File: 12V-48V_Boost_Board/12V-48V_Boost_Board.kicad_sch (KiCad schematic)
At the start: 12 parts, among them J1 12V Input, J2 Input Current Sensing, J3 Output Current Sensing, J4 48V Output, J5 Output Measuring

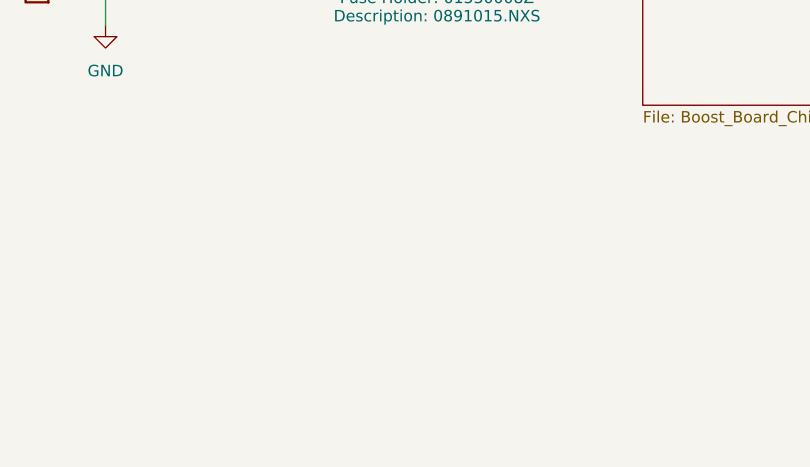
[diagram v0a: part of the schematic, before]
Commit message: Added mounting holes
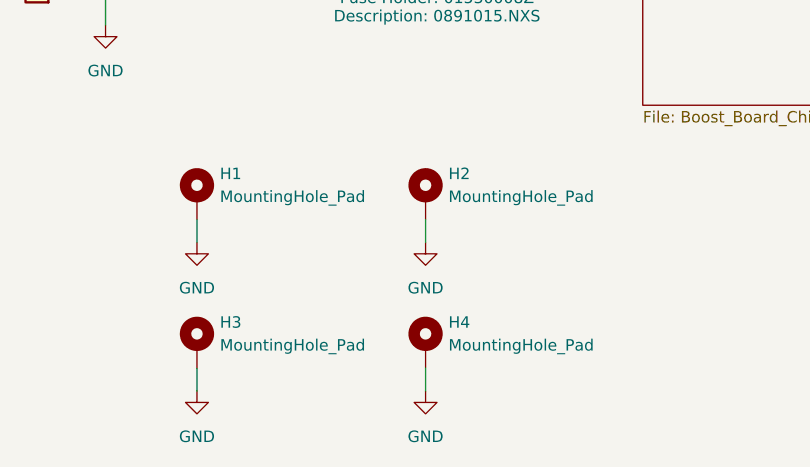
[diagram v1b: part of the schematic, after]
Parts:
- added H1, H2, H3, H4: MountingHole_Pad, MountingHole:MountingHole_3.2mm_M3_Pad, symbol Mechanical:MountingHole_Pad
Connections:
- net GND: now also H1.1, H2.1, H3.1, H4.1

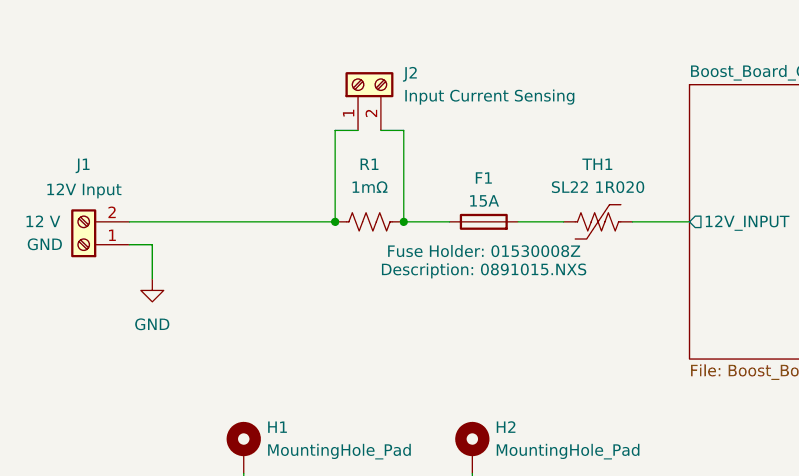
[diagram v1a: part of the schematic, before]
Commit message: Changed layout to make it more compact, changed output and input cap sizes
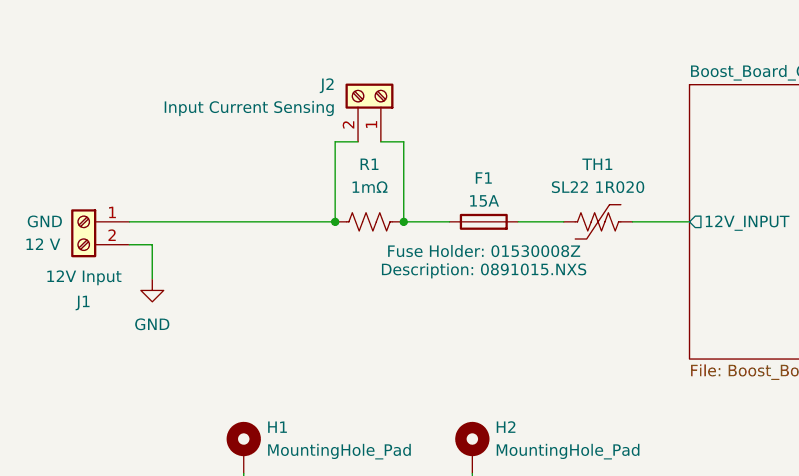
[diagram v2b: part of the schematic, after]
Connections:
- net GND: now also J1.2 (Pin_2); no longer J1.1 (Pin_1)
- net at F1.1, R1.2: now also J2.1 (Pin_1); no longer J2.2 (Pin_2)
- new net: J1.1 (Pin_1), J2.2 (Pin_2), R1.1
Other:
- moved on the sheet: J1, J2
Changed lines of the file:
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@@
 	(wire
 		(pts
-			(xy 106.68 88.9) (xy 106.68 99.06)
+			(xy 101.6 90.17) (xy 99.06 90.17)
+		)
+		(stroke
+			(width 0)
+			(type default)
+		)
+	)
+	(wire
+		(pts
+			(xy 76.2 99.06) (xy 99.06 99.06)
+		)
+		(stroke
+			(width 0)
+			(type default)
+		)
+	)
+	(wire
+		(pts
+			(xy 78.74 101.6) (xy 78.74 105.41)
+		)
+		(stroke
+			(width 0)
+			(type default)
+		)
+	)
+	(wire
+		(pts
+			(xy 106.68 90.17) (xy 106.68 99.06)
 		)
 		(stroke
@@
 	(wire
 		(pts
-			(xy 76.2 99.06) (xy 99.06 99.06)
-		)
-		(stroke
-			(width 0)
-			(type default)
-		)
-	)
-	(wire
-		(pts
 			(xy 199.39 99.06) (xy 194.31 99.06)
 		)
@@
 	(wire
 		(pts
-			(xy 101.6 88.9) (xy 99.06 88.9)
-		)
-		(stroke
-			(width 0)
-			(type default)
-		)
-	)
-	(wire
-		(pts
-			(xy 99.06 88.9) (xy 99.06 99.06)
+			(xy 99.06 90.17) (xy 99.06 99.06)
 		)
 		(stroke
@@
 	(wire
 		(pts
-			(xy 104.14 88.9) (xy 106.68 88.9)
+			(xy 104.14 90.17) (xy 106.68 90.17)
 		)
 		(stroke
@@
 	(wire
 		(pts
+			(xy 76.2 101.6) (xy 78.74 101.6)
+		)
+		(stroke
+			(width 0)
+			(type default)
+		)
+	)
+	(wire
+		(pts
 			(xy 114.3 143.51) (xy 114.3 146.05)
 		)
@@
 	(wire
 		(pts
-			(xy 78.74 101.6) (xy 78.74 105.41)
-		)
-		(stroke
-			(width 0)
-			(type default)
-		)
-	)
-	(wire
-		(pts
 			(xy 207.01 88.9) (xy 207.01 99.06)
 		)
@@
 		(pts
 			(xy 233.68 120.65) (xy 218.44 120.65)
-		)
-		(stroke
-			(width 0)
-			(type default)
-		)
-	)
-	(wire
-		(pts
-			(xy 76.2 101.6) (xy 78.74 101.6)
 		)
 		(stroke
@@
 		(on_board yes)
 		(dnp no)
-		(fields_autoplaced yes)
 		(property "Reference" "R1"
 			(at 102.87 92.71 90)
@@
 	(symbol
 		(lib_id "Connector:Screw_Terminal_01x02")
-		(at 71.12 101.6 180)
+		(at 71.12 99.06 0)
+		(mirror y)
 		(unit 1)
 		(exclude_from_sim no)
@@
 		(dnp no)
 		(property "Reference" "J1"
-			(at 71.12 92.71 0)
+			(at 71.12 107.95 0)
 			(effects
 				(font
@@
 		)
 		(property "Value" "12V Input"
-			(at 71.12 95.504 0)
+			(at 71.12 105.156 0)
 			(effects
 				(font
@@
 		)
 		(property "Footprint" "TerminalBlock_Phoenix:TerminalBlock_Phoenix_PT-1,5-2-5.0-H_1x02_P5.00mm_Horizontal"
-			(at 71.12 101.6 0)
+			(at 71.12 99.06 0)
 			(effects
 				(font
@@
 		)
 		(property "Datasheet" "~"
-			(at 71.12 101.6 0)
+			(at 71.12 99.06 0)
 			(effects
 				(font
@@
 		)
 		(property "Description" "Generic screw terminal, single row, 01x02, script generated (kicad-library-utils/schlib/autogen/connector/)"
-			(at 71.12 101.6 0)
+			(at 71.12 99.06 0)
 			(effects
 				(font
@@
 		)
 		(property "Input 1" "GND"
-			(at 66.802 101.6 0)
+			(at 66.802 99.06 0)
 			(effects
 				(font
@@
 		)
 		(property "Input 2" "12 V"
-			(at 66.548 99.06 0)
+			(at 66.548 101.6 0)
 			(effects
 				(font
@@
 	(symbol
 		(lib_id "Connector:Screw_Terminal_01x02")
-		(at 101.6 83.82 90)
+		(at 104.14 85.09 270)
+		(mirror x)
 		(unit 1)
 		(exclude_from_sim no)
@@
 		(on_board yes)
 		(dnp no)
-		(fields_autoplaced yes)
 		(property "Reference" "J2"
-			(at 106.68 82.5499 90)
+			(at 99.06 83.8199 90)
 			(effects
 				(font
@@
 		)
 		(property "Value" "Input Current Sensing"
-			(at 106.68 85.0899 90)
+			(at 99.06 86.3599 90)
 			(effects
 				(font
@@
 		)
 		(property "Footprint" "TerminalBlock_Phoenix:TerminalBlock_Phoenix_PT-1,5-2-5.0-H_1x02_P5.00mm_Horizontal"
-			(at 101.6 83.82 0)
+			(at 104.14 85.09 0)
 			(effects
 				(font
@@
 		)
 		(property "Datasheet" "~"
-			(at 101.6 83.82 0)
+			(at 104.14 85.09 0)
 			(effects
 				(font
@@
 		)
 		(property "Description" "Generic screw terminal, single row, 01x02, script generated (kicad-library-utils/schlib/autogen/connector/)"
-			(at 101.6 83.82 0)
-			(effects
-				(font
+			(at 104.14 85.09 0)
+			(effects
+				(font

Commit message: Made the two resistors bigger, will implement other changes after some discussion
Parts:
- R1: footprint Resistor_SMD:R_0805_2012Metric_Pad1.20x1.40mm_HandSolder -> 12/48 boost:WSHM28181L000FEA
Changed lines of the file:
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@@
 			)
 		)
-		(property "Footprint" "Resistor_SMD:R_0805_2012Metric_Pad1.20x1.40mm_HandSolder"
+		(property "Footprint" "12/48 boost:WSHM28181L000FEA"
 			(at 103.124 98.044 90)
 			(effects
@@
 			)
 		)
-		(property "Datasheet" "~"
+		(property "Datasheet" "WSHM28181L000FEA"
 			(at 102.87 99.06 0)
 			(effects

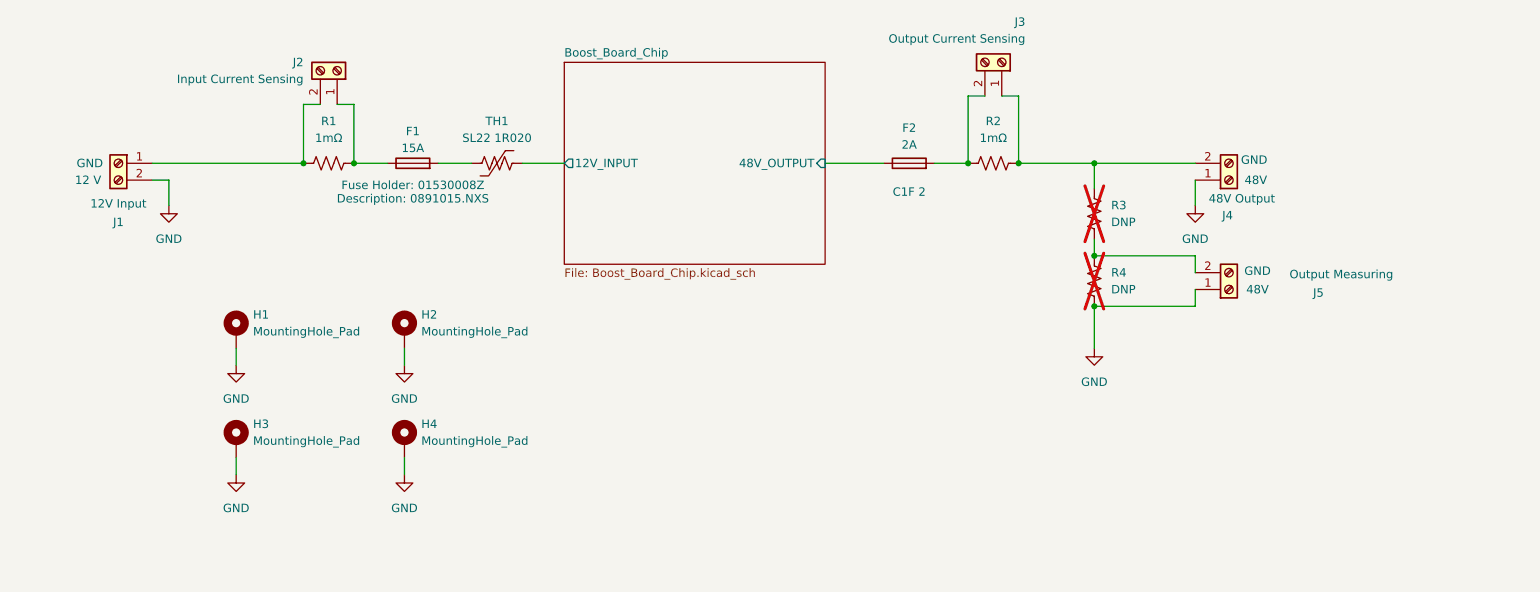
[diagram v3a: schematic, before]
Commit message: Added opamp
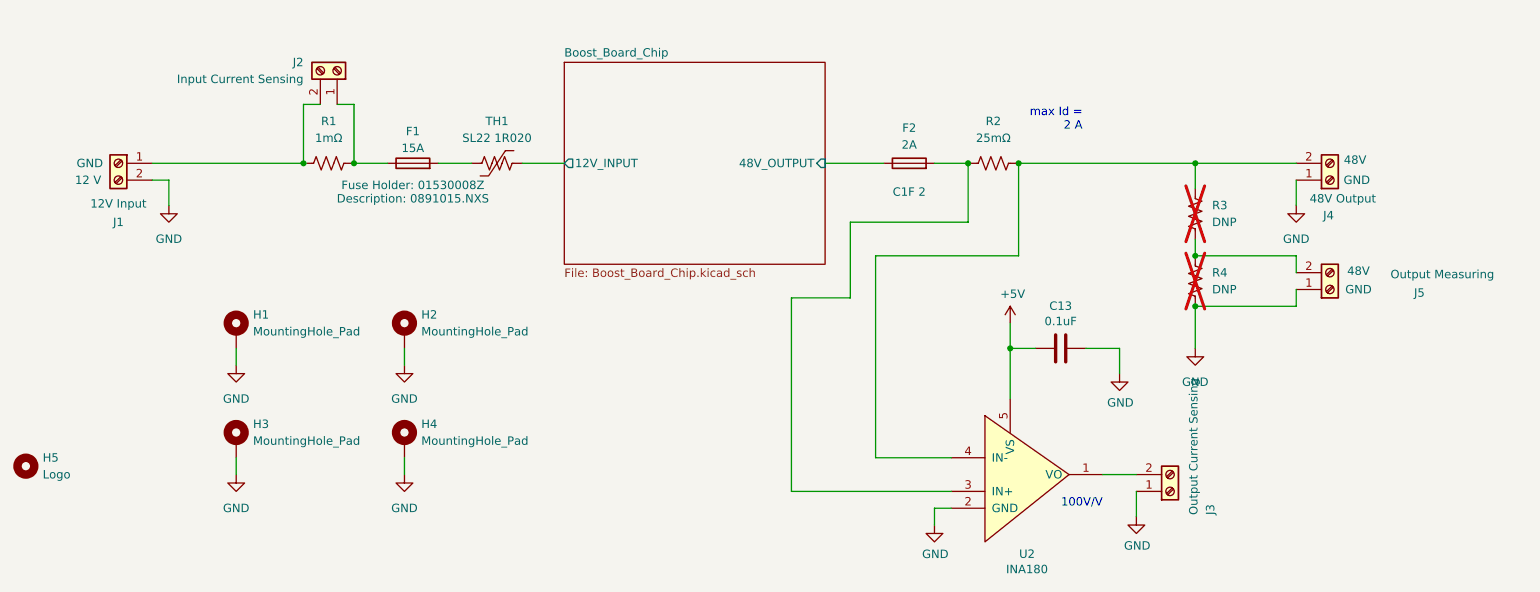
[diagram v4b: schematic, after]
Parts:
- added C13: 0.1uF, Capacitor_SMD:C_0805_2012Metric_Pad1.18x1.45mm_HandSolder, symbol Device:C
- added H5: Logo, 12/48 boost:Logo_SilkScreen_10mm, symbol Mechanical:MountingHole
- added U2: INA180, Package_TO_SOT_SMD:SOT-23-5_HandSoldering, symbol canhw:INA180
- J4: Output 1 GND -> 48V; Output 2 48V -> GND
- J5: Output 1 48V -> GND; Output 2 GND -> 48V
- R2: value 1mΩ -> 25mΩ
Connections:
- net GND: now also J3.1 (Pin_1), C13.1, U2.2 (GND)
- net at J4.2 (Pin_2), R2.2, R3.2: now also U2.4 (IN-); no longer J3.1 (Pin_1)
- net at F2.2, R2.1: now also U2.3 (IN+); no longer J3.2 (Pin_2)
- new net: J3.2 (Pin_2), U2.1 (VO)
- new net +5V: C13.2, U2.5 (VS)
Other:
- note added: "100V/V"
- note added: "max Id = 2 A"
- moved on the sheet: J3, J4, J5, R3, R4

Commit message: Changed silkscreen and vias
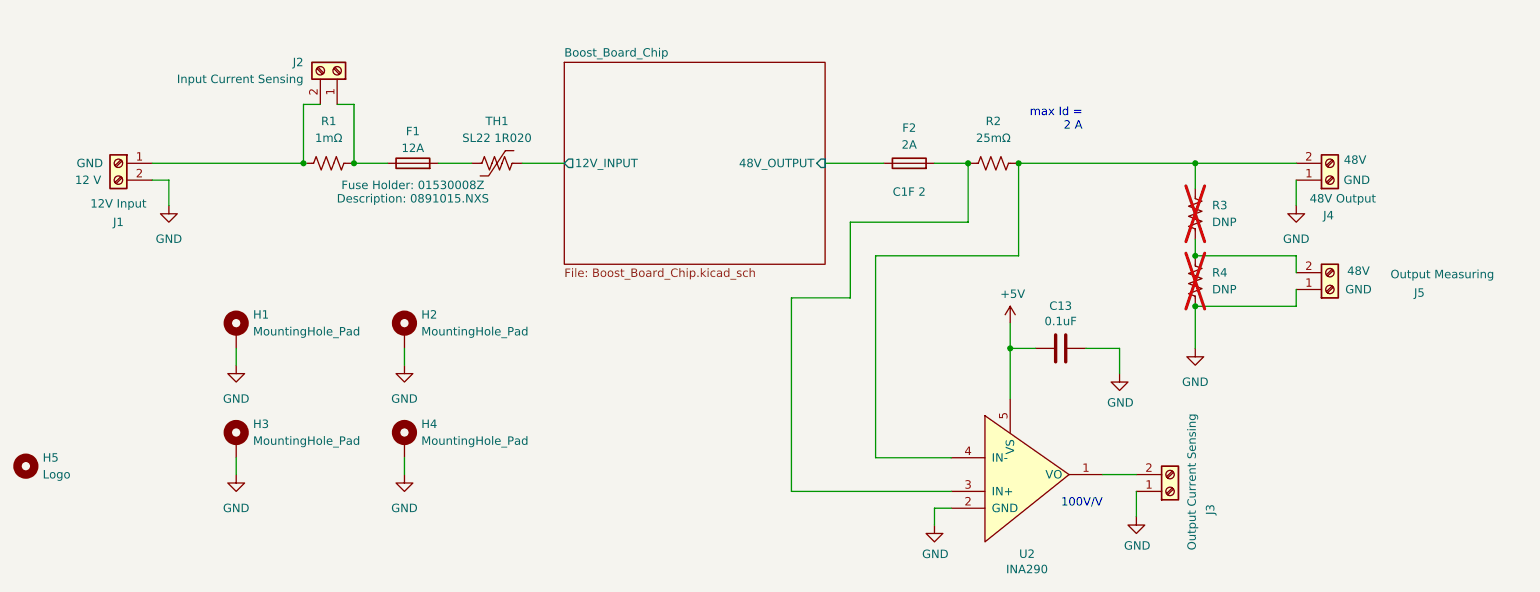
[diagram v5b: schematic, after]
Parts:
- F1: value 15A -> 12A
- U2: value INA180 -> INA290
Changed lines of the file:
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@@
 			)
 		)
-		(property "Value" "15A"
+		(property "Value" "12A"
 			(at 115.57 96.774 90)
 			(effects
@@
 			)
 		)
-		(property "Value" "INA180"
+		(property "Value" "INA290"
 			(at 208.28 160.3502 0)
 			(effects
@@
 		)
 		(property "Value" "Output Current Sensing"
-			(at 233.426 152.146 90)
-			(effects
-				(font
+			(at 233.172 157.48 90)
+			(effects
+				(font

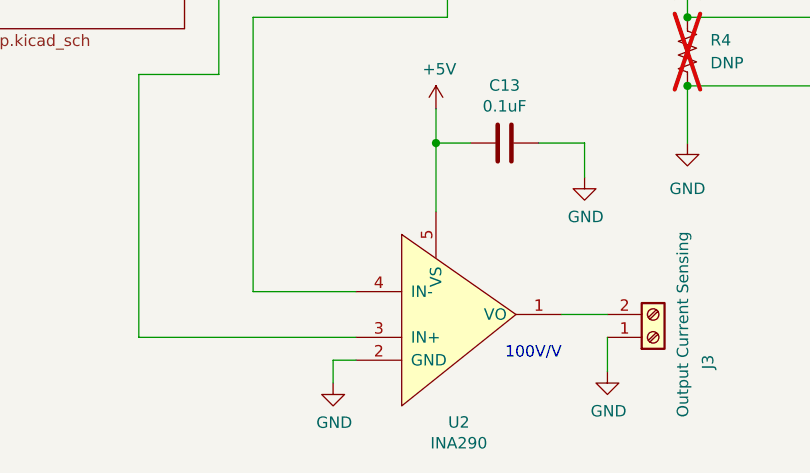
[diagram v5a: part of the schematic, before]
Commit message: Updated INA290 symbol and footprint
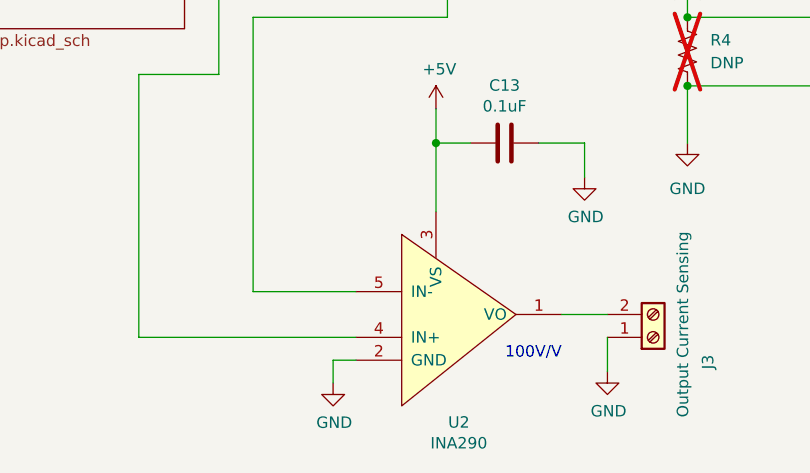
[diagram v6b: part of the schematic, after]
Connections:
- net +5V: now also U2.3 (VS); no longer U2.5 (VS)
- net at J4.2 (Pin_2), R2.2, R3.2: now also U2.5 (IN-); no longer U2.4 (IN-)
- net at F2.2, R2.1: now also U2.4 (IN+); no longer U2.3 (IN+)
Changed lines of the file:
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@@
 			)
 		)
-		(property "Datasheet" "http://www.ti.com/lit/ds/symlink/ina180.pdf"
+		(property "Datasheet" "https://www.ti.com/lit/ds/symlink/ina290.pdf"
 			(at 209.55 146.05 0)
 			(effects

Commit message: Actually updated INA290 footprint
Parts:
- U2: footprint Package_TO_SOT_SMD:SOT-23-5_HandSoldering -> 12/48 boost:SC70-5_DCK_TEX
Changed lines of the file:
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@@
 			)
 		)
-		(property "Footprint" "Package_TO_SOT_SMD:SOT-23-5_HandSoldering"
+		(property "Footprint" "12/48 boost:SC70-5_DCK_TEX"
 			(at 209.55 146.05 0)
 			(effects

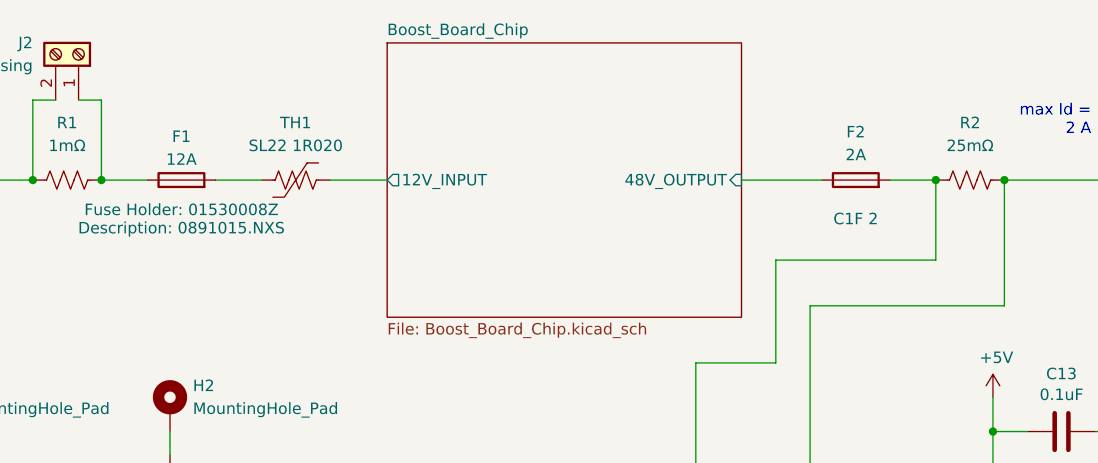
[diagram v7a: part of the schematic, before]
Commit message: Fixed the second fuse hold to be a holder
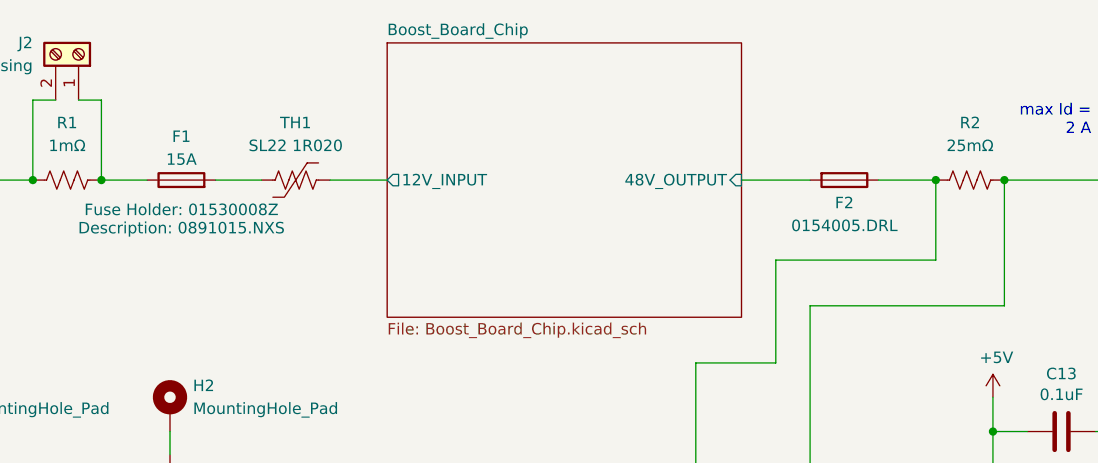
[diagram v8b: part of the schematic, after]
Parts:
- F1: value 12A -> 15A
- F2: value 2A -> 0154005.DRL; footprint Fuse:Fuse_1206_3216Metric -> 12/48 boost:0154Series_LTF
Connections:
- net Boost_Board_Chip/48V_OUTPUT: now also F2.2; no longer F2.1
- net at R2.1, U2.4 (IN+): now also F2.1; no longer F2.2
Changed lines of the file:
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@@
-	(wire
-		(pts
-			(xy 199.39 99.06) (xy 194.31 99.06)
-		)
-		(stroke
-			(width 0)
-			(type default)
-		)
-	)
 	(wire
 		(pts
@@
 	(wire
 		(pts
-			(xy 177.8 99.06) (xy 186.69 99.06)
+			(xy 193.04 99.06) (xy 199.39 99.06)
 		)
 		(stroke
@@
 		(pts
 			(xy 172.72 119.38) (xy 172.72 148.59)
+		)
+		(stroke
+			(width 0)
+			(type default)
+		)
+	)
+	(wire
+		(pts
+			(xy 177.8 99.06) (xy 185.42 99.06)
 		)
 		(stroke
@@
 			)
 		)
-		(property "Value" "12A"
+		(property "Value" "15A"
 			(at 115.57 96.774 90)
 			(effects
@@
 	)
 	(symbol
+		(lib_id "Device:Fuse")
+		(at 189.23 99.06 270)
+		(unit 1)
+		(exclude_from_sim no)
+		(in_bom yes)
+		(on_board yes)
+		(dnp no)
+		(property "Reference" "F2"
+			(at 189.23 101.6 90)
+			(effects
+				(font
+					(size 1.27 1.27)
+				)
+			)
+		)
+		(property "Value" "0154005.DRL"
+			(at 189.23 104.14 90)
+			(effects
+				(font
+					(size 1.27 1.27)
+				)
+			)
+		)
+		(property "Footprint" "12/48 boost:0154Series_LTF"
+			(at 189.23 97.282 90)
+			(effects
+				(font
+					(size 1.27 1.27)
+				)
+				(hide yes)
+			)
+		)
+		(property "Datasheet" "~"
+			(at 189.23 99.06 0)
+			(effects
+				(font
+					(size 1.27 1.27)
+				)
+				(hide yes)
+			)
+		)
+		(property "Description" "Fuse"
+			(at 189.23 99.06 0)
+			(effects
+				(font
+					(size 1.27 1.27)
+				)
+				(hide yes)
+			)
+		)
+		(pin "1"
+		)
+		(pin "2"
+		)
+		(instances
+			(project "12V-48V_Boost_Board"
+				(path "/3a220cd2-54b9-463d-ba95-4a8308a2a2d6"
+					(reference "F2")
+					(unit 1)
+				)
+			)
+		)
+	)
+	(symbol
 		(lib_id "power:GND")
 		(at 224.79 152.4 0)
@@
 					(unit 1)
 				)
-			)
-		)
-	)
-	(symbol
-		(lib_id "Device:Fuse")
-		(at 190.5 99.06 90)
-		(unit 1)
-		(exclude_from_sim yes)
-		(in_bom yes)
-		(on_board yes)
-		(dnp no)
-		(property "Reference" "F2"
-			(at 190.5 93.726 90)
-			(effects
-				(font
-					(size 1.27 1.27)
-				)
-			)
-		)
-		(property "Value" "2A"
-			(at 190.5 96.266 90)
-			(effects
-				(font
-					(size 1.27 1.27)
-				)
-			)
-		)
-		(property "Footprint" "Fuse:Fuse_1206_3216Metric"
-			(at 190.5 100.838 90)
-			(effects
-				(font
-					(size 1.27 1.27)
-				)
-				(hide yes)
-			)
-		)
-		(property "Datasheet" "https://www.digikey.ca/en/products/detail/bel-fuse-inc/C1F-2/4968250"
-			(at 190.5 99.06 0)
-			(effects
-				(font
-					(size 1.27 1.27)
-				)
-				(hide yes)
-			)
-		)
-		(property "Description" "C1F 2"
-			(at 190.5 103.378 90)
-			(effects
-				(font
-					(size 1.27 1.27)
-				)
-			)
-		)
-		(pin "1"
-		)
-		(pin "2"
-		)
-		(instances
-			(project "12V-48V_Boost_Board"
-				(path "/3a220cd2-54b9-463d-ba95-4a8308a2a2d6"
-					(reference "F2")
-					(unit 1)
-				)
